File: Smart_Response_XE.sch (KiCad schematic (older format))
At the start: 102 parts, among them J1 JTAG, J2 ISP, J3 RS232, P3 DISPLAY, Q1 NMOS ??, Q2 PZT2222A*, SW1 ON/OFF, U1 MASW-007221, U2 25LCxxx, U3 ATmega128RFA1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

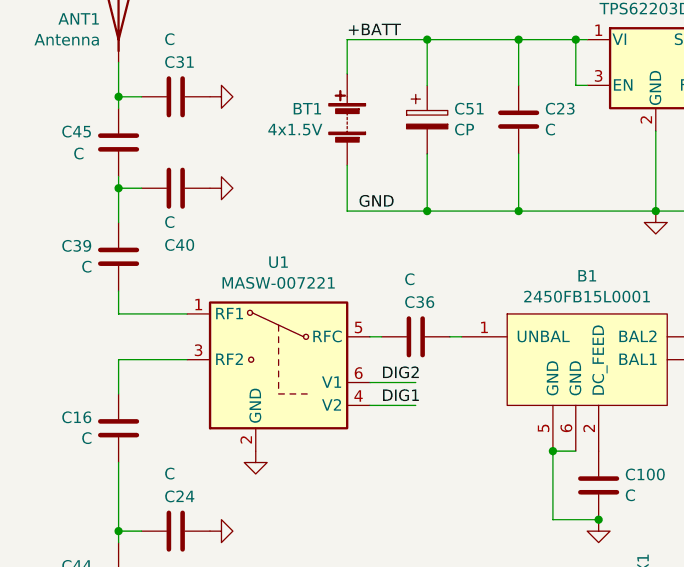
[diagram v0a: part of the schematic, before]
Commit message: Updated schematics
Added some comment
Updated reference of U1 in Smart_Response_XE.sch (and .pdf too)
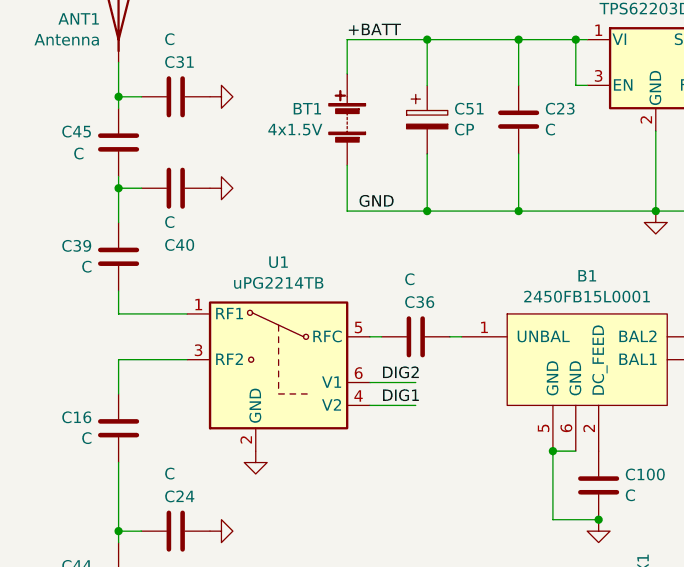
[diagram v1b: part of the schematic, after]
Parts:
- U1: value MASW-007221 -> uPG2214TB
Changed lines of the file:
@@
 EESchema Schematic File Version 4
-LIBS:Smart_Response_XE-cache
 EELAYER 30 0
 EELAYER END
@@
 P 1800 2200
 F 0 "U1" H 1800 2625 50  0000 C CNN
-F 1 "MASW-007221" H 1800 2534 50  0000 C CNN
+F 1 "uPG2214TB" H 1800 2534 50  0000 C CNN
 F 2 "Package_TO_SOT_SMD:SOT-363_SC-70-6" H 1800 2300 50  0001 C CNN
 F 3 "http://cdn.macom.com/datasheets/masw-007221.pdf" H 1800 2300 50  0001 C CNN

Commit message: Migrate library cache to project-local library
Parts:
- B1: symbol MyDevices:2450FB15L0001 -> srxe:2450FB15L0001-MyDevices
- SW1: symbol MyDevices:SW_push_small -> srxe:SW_push_small-MyDevices
- U3: symbol MyDevices:ATmega128RFA1 -> srxe:ATmega128RFA1-MyDevices
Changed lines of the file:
@@
 $EndDescr
 $Comp
-L MyDevices:ATmega128RFA1 U3
+L srxe:ATmega128RFA1-MyDevices U3
 U 1 1 5DB731A8
 P 5100 1800
@@
 $EndComp
 $Comp
-L MyDevices:2450FB15L0001 B1
+L srxe:2450FB15L0001-MyDevices B1
 U 1 2 5DBAEC6F
 P 3100 1900
@@
 Connection ~ 8000 3950
 $Comp
-L MyDevices:SW_push_small SW1
+L srxe:SW_push_small-MyDevices SW1
 U 1 1 5E5ED506
 P 7550 3100

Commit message: Move peripherals to a separate sheet.
This is to increase real estate necessary for filling in
some missing components.
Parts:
- removed C18: C, symbol Device:C
- removed C30, C33, C41, C42, C43: C*, symbol Device:C
- removed D1: D*, symbol Device:D
- removed D2: LED*, symbol Device:LED
- removed J3: RS232, symbol Connector_Generic:Conn_02x03_Odd_Even
- removed Q1: NMOS ??, symbol Device:Q_NMOS_GSD
- removed Q2: PZT2222A*, Package_TO_SOT_SMD:SOT-223, symbol Transistor_BJT:PZT2222A
- removed R10, R14, R18, R34, R35, R36, R37, R39, R9: R*, symbol Device:R_Small
- removed R16, R17: 10k, symbol Device:R_Small
- removed R21, R28: 0, symbol Device:R_Small
- removed R3: 33, symbol Device:R_Small
- removed SP1: Buzzer*, symbol Device:Buzzer
- removed U2: 25LCxxx, symbol Memory_EEPROM:25LCxxx
- removed U5: Mystery comp, symbol Connector_Generic:Conn_02x05_Counter_Clockwise
- removed U6: MAX3226*, Package_SO:SSOP-16_5.3x6.2mm_P0.65mm, symbol Interface_UART:MAX3226
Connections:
- net labels removed: CS_U5, SCL, SDA
- wire segments 373 -> 314
- no-connect marks 7 -> 4
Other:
- note removed: "Debug"
- moved on the sheet: C17, C27, C28, C6, C7, C8, CX3, CX4, FB1, J1, J2, P3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

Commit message: Add missing components, mostly around Mystery U5 IC.
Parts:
- removed R41: 0, symbol Device:R_Small
- removed R42: R*, symbol Device:R_Small
- added R41: Jumper_2_Bridged, symbol Jumper:Jumper_2_Bridged
- added R42: Jumper_2_Open, symbol Jumper:Jumper_2_Open
- added Z1: D_Zener_x2_ACom_KAK, symbol Device:D_Zener_x2_ACom_KAK
- C24, C29, C40: value C -> C*
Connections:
- wire segments 314 -> 316
- no-connect marks 4 -> 5
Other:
- moved on the sheet: R1
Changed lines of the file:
@@
 L power:GND #PWR0107
 U 1 1 5DBEEC9D
-P 6950 2500
-F 0 "#PWR0107" H 6950 2250 50  0001 C CNN
-F 1 "GND" H 6950 2350 50  0001 C CNN
-F 2 "" H 6950 2500 50  0001 C CNN
-F 3 "" H 6950 2500 50  0001 C CNN
-	1    6950 2500
+P 6950 2800
+F 0 "#PWR0107" H 6950 2550 50  0001 C CNN
+F 1 "GND" H 6950 2650 50  0001 C CNN
+F 2 "" H 6950 2800 50  0001 C CNN
+F 3 "" H 6950 2800 50  0001 C CNN
+	1    6950 2800
 	1    0    0    -1
 $EndComp
@@
 P 1350 1450
 F 0 "C40" V 1100 1400 50  0000 L CNN
-F 1 "C" V 1200 1400 50  0000 L CNN
+F 1 "C*" V 1200 1400 50  0000 L CNN
 F 2 "" H 1388 1300 50  0001 C CNN
 F 3 "~" H 1350 1450 50  0001 C CNN
@@
 P 1350 2950
 F 0 "C24" V 1500 2900 50  0000 L CNN
-F 1 "C" V 1600 2900 50  0000 L CNN
+F 1 "C*" V 1600 2900 50  0000 L CNN
 F 2 "" H 1388 2800 50  0001 C CNN
 F 3 "~" H 1350 2950 50  0001 C CNN
@@
 P 1350 3350
 F 0 "C29" V 1100 3300 50  0000 L CNN
-F 1 "C" V 1200 3300 50  0000 L CNN
+F 1 "C*" V 1200 3300 50  0000 L CNN
 F 2 "" H 1388 3200 50  0001 C CNN
 F 3 "~" H 1350 3350 50  0001 C CNN
@@
 L srxe:SW_push_small-MyDevices SW1
 U 1 1 5E5ED506
-P 6950 2100
-F 0 "SW1" H 7078 1896 50  0000 L CNN
-F 1 "ON/OFF" H 7078 1805 39  0000 L CNN
-F 2 "" H 6950 2100 50  0001 C CNN
-F 3 "" H 6950 2100 50  0001 C CNN
-	1    6950 2100
+P 6950 2400
+F 0 "SW1" H 7078 2196 50  0000 L CNN
+F 1 "ON/OFF" H 7078 2105 39  0000 L CNN
+F 2 "" H 6950 2400 50  0001 C CNN
+F 3 "" H 6950 2400 50  0001 C CNN
+	1    6950 2400
 	1    0    0    -1
 $EndComp
@@
 L Device:R_Small R1
 U 1 1 5E704A52
-P 6950 2000
-F 0 "R1" V 7050 1950 50  0000 L CNN
-F 1 "47k" V 6850 1950 50  0000 L CNN
-F 2 "" H 6950 2000 50  0001 C CNN
-F 3 "~" H 6950 2000 50  0001 C CNN
-	1    6950 2000
+P 6950 2300
+F 0 "R1" V 7050 2250 50  0000 L CNN
+F 1 "47k" V 6850 2250 50  0000 L CNN
+F 2 "" H 6950 2300 50  0001 C CNN
+F 3 "~" H 6950 2300 50  0001 C CNN
+	1    6950 2300
 	1    0    0    1
 $EndComp
@@
 L power:+3.3V #PWR0144
 U 1 1 5E75C15D
-P 6950 1900
-F 0 "#PWR0144" H 6950 1750 50  0001 C CNN
-F 1 "+3.3V" H 6950 2050 50  0000 C CNN
-F 2 "" H 6950 1900 50  0001 C CNN
-F 3 "" H 6950 1900 50  0001 C CNN
-	1    6950 1900
+P 6950 2200
+F 0 "#PWR0144" H 6950 2050 50  0001 C CNN
+F 1 "+3.3V" H 6950 2350 50  0000 C CNN
+F 2 "" H 6950 2200 50  0001 C CNN
+F 3 "" H 6950 2200 50  0001 C CNN
+	1    6950 2200
 	1    0    0    -1
 $EndComp
@@
 Text Label 6400 4600 2    50   ~ 0
 COL1
-$Comp
-L Device:R_Small R41
-U 1 1 5DC0DC13
-P 8450 2450
-F 0 "R41" H 8250 2500 50  0000 L CNN
-F 1 "0" H 8350 2400 50  0000 L CNN
-F 2 "" H 8450 2450 50  0001 C CNN
-F 3 "~" H 8450 2450 50  0001 C CNN
-	1    8450 2450
-	-1   0    0    -1
-$EndComp
 Wire Wire Line
 	3900 5800 4000 5800
@@
 Wire Wire Line
 	6400 2000 6100 2000
-$Comp
-L Device:R_Small R42
-U 1 1 5DE23AF9
-P 8750 2450
-F 0 "R42" H 8800 2400 50  0000 L CNN
-F 1 "R*" H 8800 2500 50  0000 L CNN
-F 2 "" H 8750 2450 50  0001 C CNN
-F 3 "~" H 8750 2450 50  0001 C CNN
-	1    8750 2450
-	1    0    0    1
-$EndComp
 $Comp
 L power:GND #PWR0159
@@
 F10 "SDA" I L 9900 2100 50
 F11 "SCL" I L 9900 2000 50
-F12 "U5_CS" I L 9900 2200 50
-F13 "DEBUG" I L 9900 850 50
+F12 "DEBUG" I L 9900 850 50
+F13 "U5_INT" I L 9900 2200 50
 $EndSheet
 Wire Wire Line
@@
 RST
 Wire Wire Line
-	6950 2100 6950 2150
-Wire Wire Line
-	6950 2150 6750 2150
-Wire Wire Line
-	6750 2150 6750 3200
-Connection ~ 6950 2150
-Wire Wire Line
-	6950 2150 6950 2200
+	6950 2400 6950 2450
+Wire Wire Line
+	6950 2450 6750 2450
+Connection ~ 6950 2450
+Wire Wire Line
+	6950 2450 6950 2500
 $Comp
 L power:+3.3V #PWR0102
@@
 	6150 4450 8450 4450
 Wire Wire Line
-	8450 4450 8450 2700
-Wire Wire Line
 	6150 4450 6150 4600
 Wire Wire Line
-	8450 2100 8450 2350
+	8450 2100 8450 2300
 Connection ~ 8450 2100
 Wire Wire Line
@@
 	6100 3100 7500 3100
 Wire Wire Line
-	8750 2550 8750 2700
-Wire Wire Line
-	8750 2700 8450 2700
-Connection ~ 8450 2700
-Wire Wire Line
-	8450 2700 8450 2550
-Wire Wire Line
-	8750 2350 8750 850
+	8750 2300 8750 850
 Connection ~ 8750 850
 Wire Wire Line
@@
 	0    1    -1   0
 $EndComp
+$Comp
+L Jumper:Jumper_2_Open R42
+U 1 1 63E61B9E
+P 8750 2500
+F 0 "R42" V 8750 2598 50  0000 L CNN
+F 1 "Jumper_2_Open" V 8795 2598 50  0001 L CNN
+F 2 "" H 8750 2500 50  0001 C CNN
+F 3 "~" H 8750 2500 50  0001 C CNN
+	1    8750 2500
+	0    1    1    0
+$EndComp
+Wire Wire Line
+	8750 2700 8750 2800
+Wire Wire Line
+	8750 2800 8450 2800
+Wire Wire Line
+	8450 2800 8450 4450
+$Comp
+L Jumper:Jumper_2_Bridged R41
+U 1 1 63F0A72A
+P 8450 2500
+F 0 "R41" V 8450 2558 50  0000 L CNN
+F 1 "Jumper_2_Bridged" V 8495 2558 50  0001 L CNN
+F 2 "" H 8450 2500 50  0001 C CNN
+F 3 "~" H 8450 2500 50  0001 C CNN
+	1    8450 2500
+	0    1    1    0
+$EndComp
+Wire Wire Line
+	8450 2700 8450 2800
+Connection ~ 8450 2800
+$Comp
+L Device:D_Zener_x2_ACom_KAK Z1
+U 1 1 63F939ED
+P 7100 1450
+F 0 "Z1" H 7100 1575 50  0000 C CNN
+F 1 "D_Zener_x2_ACom_KAK" H 7100 1575 50  0001 C CNN
+F 2 "" H 7100 1450 50  0001 C CNN
+F 3 "~" H 7100 1450 50  0001 C CNN
+	1    7100 1450
+	1    0    0    -1
+$EndComp
+Connection ~ 6750 2450
+Wire Wire Line
+	6750 2450 6750 3200
+Wire Wire Line
+	6750 1450 6750 2450
+$Comp
+L power:GND #PWR?
+U 1 1 63FD1C8A
+P 7100 1650
+F 0 "#PWR?" H 7100 1400 50  0001 C CNN
+F 1 "GND" H 7105 1477 50  0000 C CNN
+F 2 "" H 7100 1650 50  0001 C CNN
+F 3 "" H 7100 1650 50  0001 C CNN
+	1    7100 1650
+	1    0    0    -1
+$EndComp
+Wire Wire Line
+	6750 1450 6800 1450
+NoConn ~ 7400 1450
 $EndSCHEMATC

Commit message: Fill in more missing components
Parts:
- removed R2: R*, symbol Device:R_Small
- added R2: Jumper_2_Open, symbol Jumper:Jumper_2_Open
- added TP17: V3P3, symbol Connector:TestPoint
- C22, C32: value C -> C*
- R20: value R -> R*
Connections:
- net labels removed: EXT, VPP
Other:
- moved on the sheet: C7, R29, R30, R31
